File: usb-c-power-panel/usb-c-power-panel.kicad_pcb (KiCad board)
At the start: 2 copper layers, 25 x 14.1 mm, 3 parts

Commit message: usb c power mvp
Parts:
- removed the REF** at (110.1, 94.9)
- removed the REF** at (120.0, 107.0)
- removed the REF** at (105.0, 107.0)
- added REF**: MountingHole_1mm, MountingHoleSmall:MountingHole_1mm, F.Cu at (115.0, 109.1)
- added REF**: MountingHole_1mm, MountingHoleSmall:MountingHole_1mm, F.Cu at (111.3, 105.0)
- added REF**: MountingHole_1mm, MountingHoleSmall:MountingHole_1mm, F.Cu at (110.0, 105.0)
- added REF**: MountingHole_1mm, MountingHoleSmall:MountingHole_1mm, F.Cu at (115.0, 105.0)
- added REF**: MountingHole_1mm, MountingHoleSmall:MountingHole_1mm, F.Cu at (112.5, 109.1)
- added REF**: MountingHole_1mm, MountingHoleSmall:MountingHole_1mm, F.Cu at (112.5, 105.0)
- added REF**: MountingHole_1mm, MountingHoleSmall:MountingHole_1mm, F.Cu at (117.5, 107.7)
- added REF**: MountingHole_1mm, MountingHoleSmall:MountingHole_1mm, F.Cu at (107.5, 107.7)
- added REF**: MountingHole_1mm, MountingHoleSmall:MountingHole_1mm, F.Cu at (117.5, 106.4)
- added REF**: MountingHole_1mm, MountingHoleSmall:MountingHole_1mm, F.Cu at (107.5, 106.4)
- added REF**: MountingHole_1mm, MountingHoleSmall:MountingHole_1mm, F.Cu at (117.5, 109.1)
- added REF**: MountingHole_1mm, MountingHoleSmall:MountingHole_1mm, F.Cu at (110.0, 109.1)
- added REF**: MountingHole_1mm, MountingHoleSmall:MountingHole_1mm, F.Cu at (117.5, 105.0)
- added REF**: MountingHole_1mm, MountingHoleSmall:MountingHole_1mm, F.Cu at (107.5, 109.1)
- added REF**: MountingHole_1mm, MountingHoleSmall:MountingHole_1mm, F.Cu at (107.5, 105.0)
- added REF**: MountingHole_1mm, MountingHoleSmall:MountingHole_1mm, F.Cu at (120.0, 107.0)
- added REF**: MountingHole_1mm, MountingHoleSmall:MountingHole_1mm, F.Cu at (105.0, 107.0)
- added REF**: MountingHole_1mm, MountingHoleSmall:MountingHole_1mm, F.Cu at (111.3, 109.1)
- added REF**: MountingHole_1mm, MountingHoleSmall:MountingHole_1mm, F.Cu at (113.7, 109.1)
- added REF**: MountingHole_1mm, MountingHoleSmall:MountingHole_1mm, F.Cu at (116.2, 109.1)
- added REF**: MountingHole_1mm, MountingHoleSmall:MountingHole_1mm, F.Cu at (108.8, 109.1)
- added REF**: MountingHole_1mm, MountingHoleSmall:MountingHole_1mm, F.Cu at (108.8, 105.0)
- added REF**: MountingHole_1mm, MountingHoleSmall:MountingHole_1mm, F.Cu at (116.2, 105.0)
- added REF**: MountingHole_1mm, MountingHoleSmall:MountingHole_1mm, F.Cu at (113.7, 105.0)

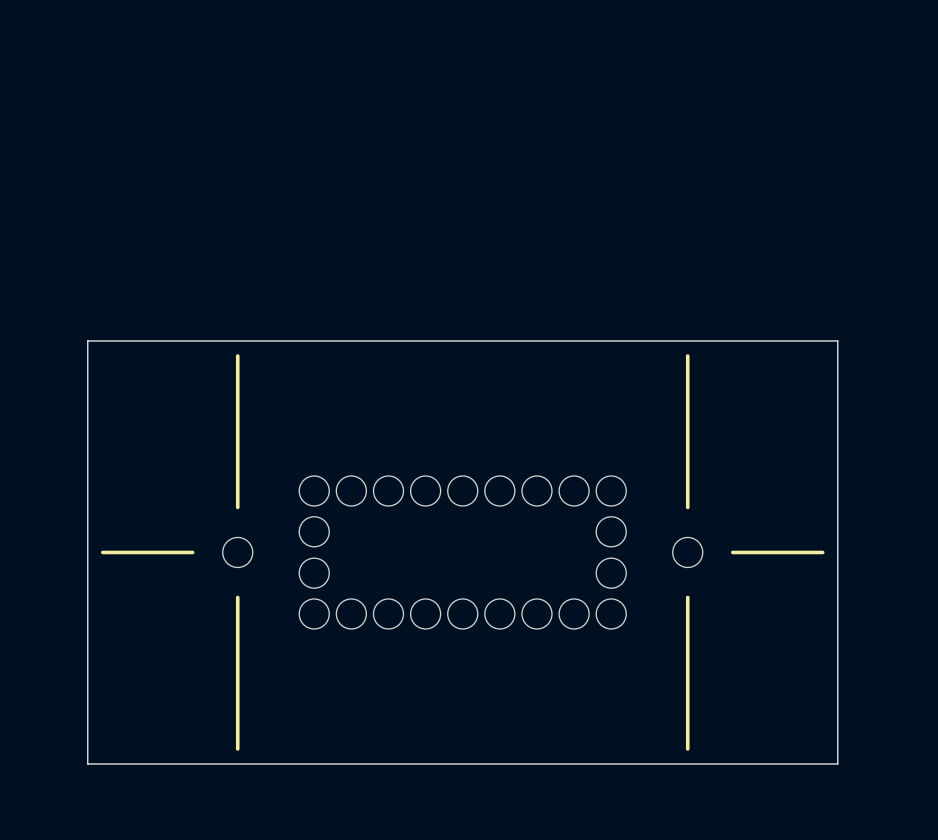
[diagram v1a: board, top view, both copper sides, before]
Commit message: usb c power finished
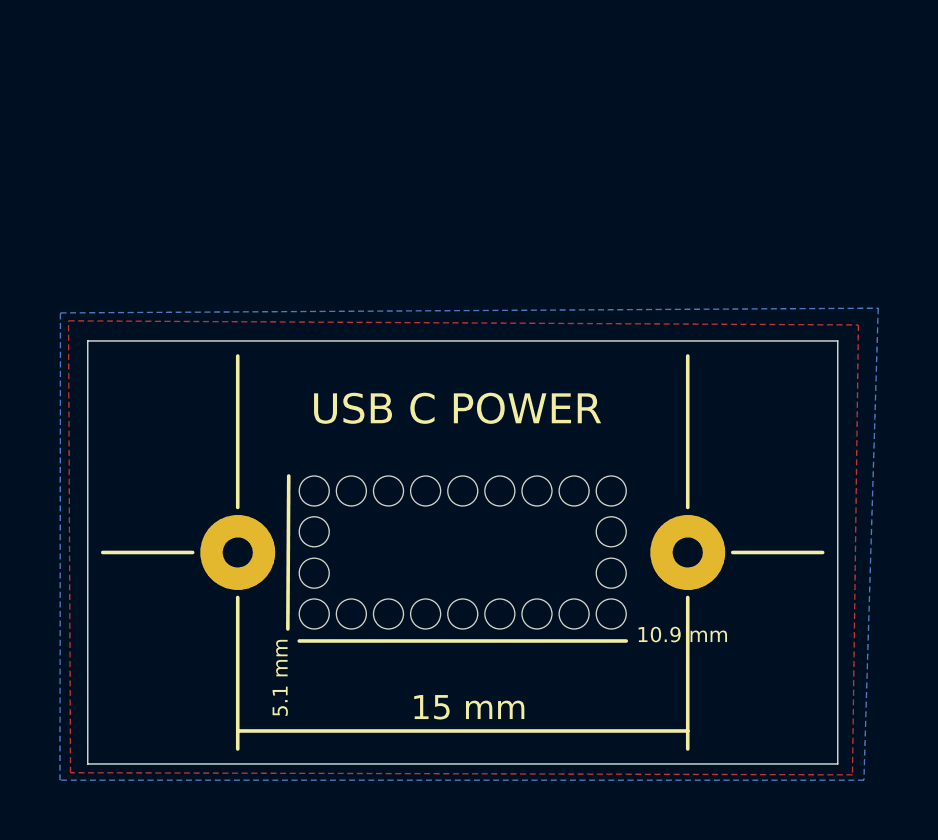
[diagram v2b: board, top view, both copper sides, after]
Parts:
- removed the REF** at (120.0, 107.0)
- removed the REF** at (105.0, 107.0)
- added REF**: SolderWirePad_1x01_Drill1mm, Connector_Wire:SolderWirePad_1x01_Drill1mm, F.Cu at (120.0, 107.0)
- added REF**: SolderWirePad_1x01_Drill1mm, Connector_Wire:SolderWirePad_1x01_Drill1mm, F.Cu at (105.0, 107.0)
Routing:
- added copper zone on B.Cu, net (none)
- added copper zone on F.Cu, net (none)
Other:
- board text added: "10.9 mm"
- board text added: "15 mm"
- board text added: "5.1 mm"
- board text added: "USB C POWER"
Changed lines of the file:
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@@
   (general
     (thickness 1.6)
-    (drawings 10)
+    (drawings 17)
     (tracks 0)
     (zones 0)
@@
     (uvia_drill 0.1)
   )
+  (module Connector_Wire:SolderWirePad_1x01_Drill1mm (layer F.Cu)
+    (at 120 107.05)
+    (descr "Wire solder connection")
+    (tags connector)
+    (attr virtual)
+    (fp_text reference REF** (at 0 -3.81) (layer F.SilkS) hide
+      (effects (font (size 1 1) (thickness 0.15)))
+    )
+    (fp_text value SolderWirePad_1x01_Drill1mm (at 0 3.175) (layer F.Fab) hide
+      (effects (font (size 1 1) (thickness 0.15)))
+    )
+    (fp_text user %R (at 0 0) (layer F.Fab) hide
+      (effects (font (size 1 1) (thickness 0.15)))
+    )
+    (fp_line (start -1.75 -1.75) (end 1.75 -1.75) (layer F.CrtYd) (width 0.05))
+    (fp_line (start -1.75 -1.75) (end -1.75 1.75) (layer F.CrtYd) (width 0.05))
+    (fp_line (start 1.75 1.75) (end 1.75 -1.75) (layer F.CrtYd) (width 0.05))
+    (fp_line (start 1.75 1.75) (end -1.75 1.75) (layer F.CrtYd) (width 0.05))
+    (pad 1 thru_hole circle (at 0 0) (size 2.49936 2.49936) (drill 1.00076) (layers *.Cu *.Mask))
+  )
+  (module Connector_Wire:SolderWirePad_1x01_Drill1mm (layer F.Cu)
+    (at 105 107.05)
+    (descr "Wire solder connection")
+    (tags connector)
+    (attr virtual)
+    (fp_text reference REF** (at 0 -3.81) (layer F.SilkS) hide
+      (effects (font (size 1 1) (thickness 0.15)))
+    )
+    (fp_text value SolderWirePad_1x01_Drill1mm (at 0 3.175) (layer F.Fab) hide
+      (effects (font (size 1 1) (thickness 0.15)))
+    )
+    (fp_line (start 1.75 1.75) (end -1.75 1.75) (layer F.CrtYd) (width 0.05))
+    (fp_line (start 1.75 1.75) (end 1.75 -1.75) (layer F.CrtYd) (width 0.05))
+    (fp_line (start -1.75 -1.75) (end -1.75 1.75) (layer F.CrtYd) (width 0.05))
+    (fp_line (start -1.75 -1.75) (end 1.75 -1.75) (layer F.CrtYd) (width 0.05))
+    (fp_text user %R (at 0 0) (layer F.Fab) hide
+      (effects (font (size 1 1) (thickness 0.15)))
+    )
+    (pad 1 thru_hole circle (at 0 0) (size 2.49936 2.49936) (drill 1.00076) (layers *.Cu *.Mask))
+  )
   (module MountingHoleSmall:MountingHole_1mm (layer F.Cu)
     (at 114.975 109.1)
@@
     (pad "" np_thru_hole circle (at 0 0) (size 1 1) (drill 1) (layers *.Cu *.Mask))
   )
-  (module MountingHoleSmall:MountingHole_1mm (layer F.Cu)
-    (at 120 107.05)
-    (descr "MountingHole_1mm, no annular")
-    (tags "mountingHole_1mm no annular")
-    (attr virtual)
-    (fp_text reference REF** (at 0 -3.2) (layer F.SilkS) hide
-      (effects (font (size 1 1) (thickness 0.15)))
-    )
-    (fp_text value MountingHole_1mm (at 0 3.2) (layer F.Fab) hide
-      (effects (font (size 1 1) (thickness 0.15)))
-    )
-    (fp_text user %R (at 0.3 0) (layer F.Fab) hide
-      (effects (font (size 1 1) (thickness 0.15)))
-    )
-    (fp_circle (center 0 0) (end 1 0) (layer Cmts.User) (width 0.15))
-    (fp_circle (center 0 0) (end 1.25 0) (layer F.CrtYd) (width 0.05))
-    (pad "" np_thru_hole circle (at 0 0) (size 1 1) (drill 1) (layers *.Cu *.Mask))
-  )
-  (module MountingHoleSmall:MountingHole_1mm (layer F.Cu)
-    (at 105 107.05)
-    (descr "MountingHole_1mm, no annular")
-    (tags "mountingHole_1mm no annular")
-    (attr virtual)
-    (fp_text reference REF** (at 0 -3.2) (layer F.SilkS) hide
-      (effects (font (size 1 1) (thickness 0.15)))
-    )
-    (fp_text value MountingHole_1mm (at 0 3.2) (layer F.Fab) hide
-      (effects (font (size 1 1) (thickness 0.15)))
-    )
-    (fp_circle (center 0 0) (end 1.25 0) (layer F.CrtYd) (width 0.05))
-    (fp_circle (center 0 0) (end 1 0) (layer Cmts.User) (width 0.15))
-    (fp_text user %R (at 0.3 0) (layer F.Fab) hide
-      (effects (font (size 1 1) (thickness 0.15)))
-    )
-    (pad "" np_thru_hole circle (at 0 0) (size 1 1) (drill 1) (layers *.Cu *.Mask))
+  (gr_line (start 105 113) (end 120 113) (layer F.SilkS) (width 0.12))
+  (gr_text "10.9 mm" (at 119.82704 109.8042) (layer F.SilkS)
+    (effects (font (size 0.5 0.5) (thickness 0.125)))
+  )
+  (gr_line (start 107.05 110) (end 117.95 110) (layer F.SilkS) (width 0.12))
+  (gr_line (start 106.7 104.5) (end 106.67 109.6) (layer F.SilkS) (width 0.12))
+  (gr_text "5.1 mm" (at 106.43108 111.2266 90) (layer F.SilkS)
+    (effects (font (size 0.5 0.5) (thickness 0.125)))
+  )
+  (gr_text "15 mm" (at 112.70488 112.23244) (layer F.SilkS)
+    (effects (font (size 0.8 0.8) (thickness 0.15)))
+  )
+  (gr_text "USB C POWER" (at 112.28832 102.28072) (layer F.SilkS)
+    (effects (font (size 1 1) (thickness 0.15)))
   )
   (gr_line (start 120 108.55) (end 120 113.6) (layer F.SilkS) (width 0.12))
@@
   (gr_line (start 100 114.1) (end 125 114.1) (layer Edge.Cuts) (width 0.05))
   (gr_line (start 100 100) (end 125 100) (layer Edge.Cuts) (width 0.05))
+  (zone (net 0) (net_name "") (layer F.Cu) (hatch edge 0.508)
+    (connect_pads (clearance 0.508))
+    (min_thickness 0.254)
+    (fill yes (arc_segments 32) (thermal_gap 0.508) (thermal_bridge_width 0.508))
+    (polygon
+      (pts
+        (xy 125.68936 99.4664) (xy 125.49124 114.46256) (xy 99.42576 114.39144) (xy 99.35972 99.32924)
+      )
+    )
+  )
+  (zone (net 0) (net_name "") (layer B.Cu) (hatch edge 0.508)
+    (connect_pads (clearance 0.508))
+    (min_thickness 0.254)
+    (fill yes (arc_segments 32) (thermal_gap 0.508) (thermal_bridge_width 0.508))
+    (polygon
+      (pts
+        (xy 125.87224 114.64036) (xy 99.07524 114.64036) (xy 99.09048 99.06508) (xy 126.34976 98.9076)
+      )
+    )
+  )
 )
